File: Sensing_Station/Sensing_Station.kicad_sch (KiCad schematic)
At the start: 18 parts, among them J1 Conn_01x06_Pin, SW1 SW_Reed, U1 TMP35xS, U2 TLV172IDCK, U3 TLV172IDCK, U4 TLV172IDCK

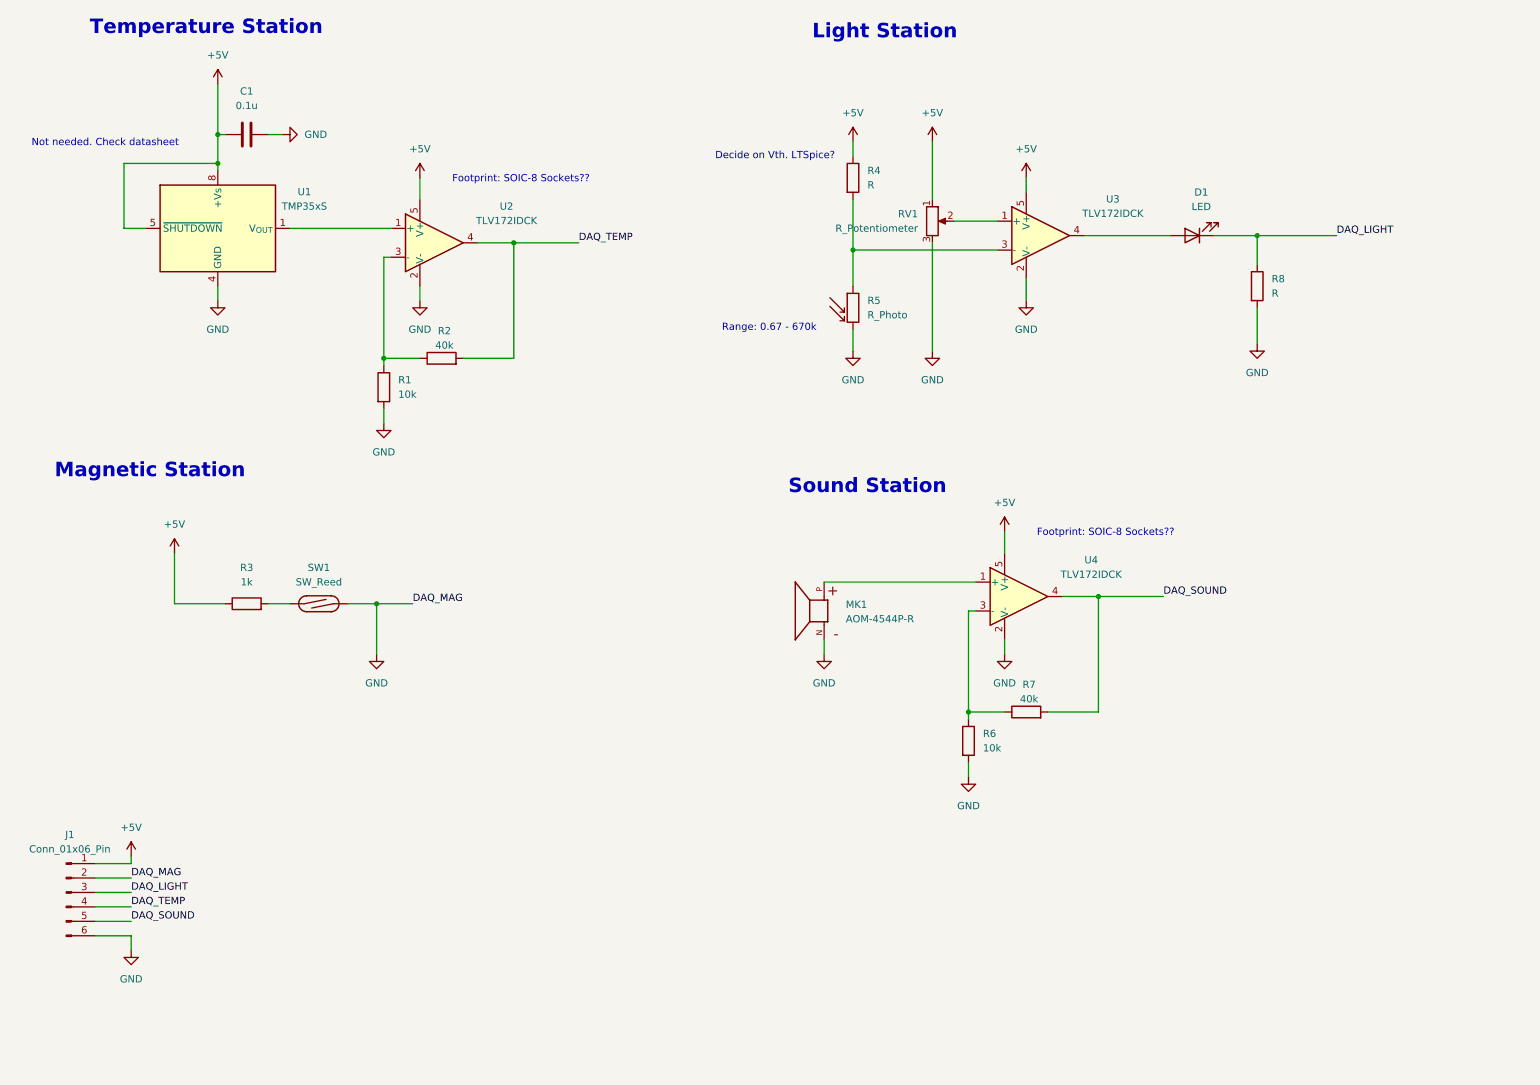
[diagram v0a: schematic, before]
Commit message: Añadido comparador doble y cambios. Falta BOM y listado final
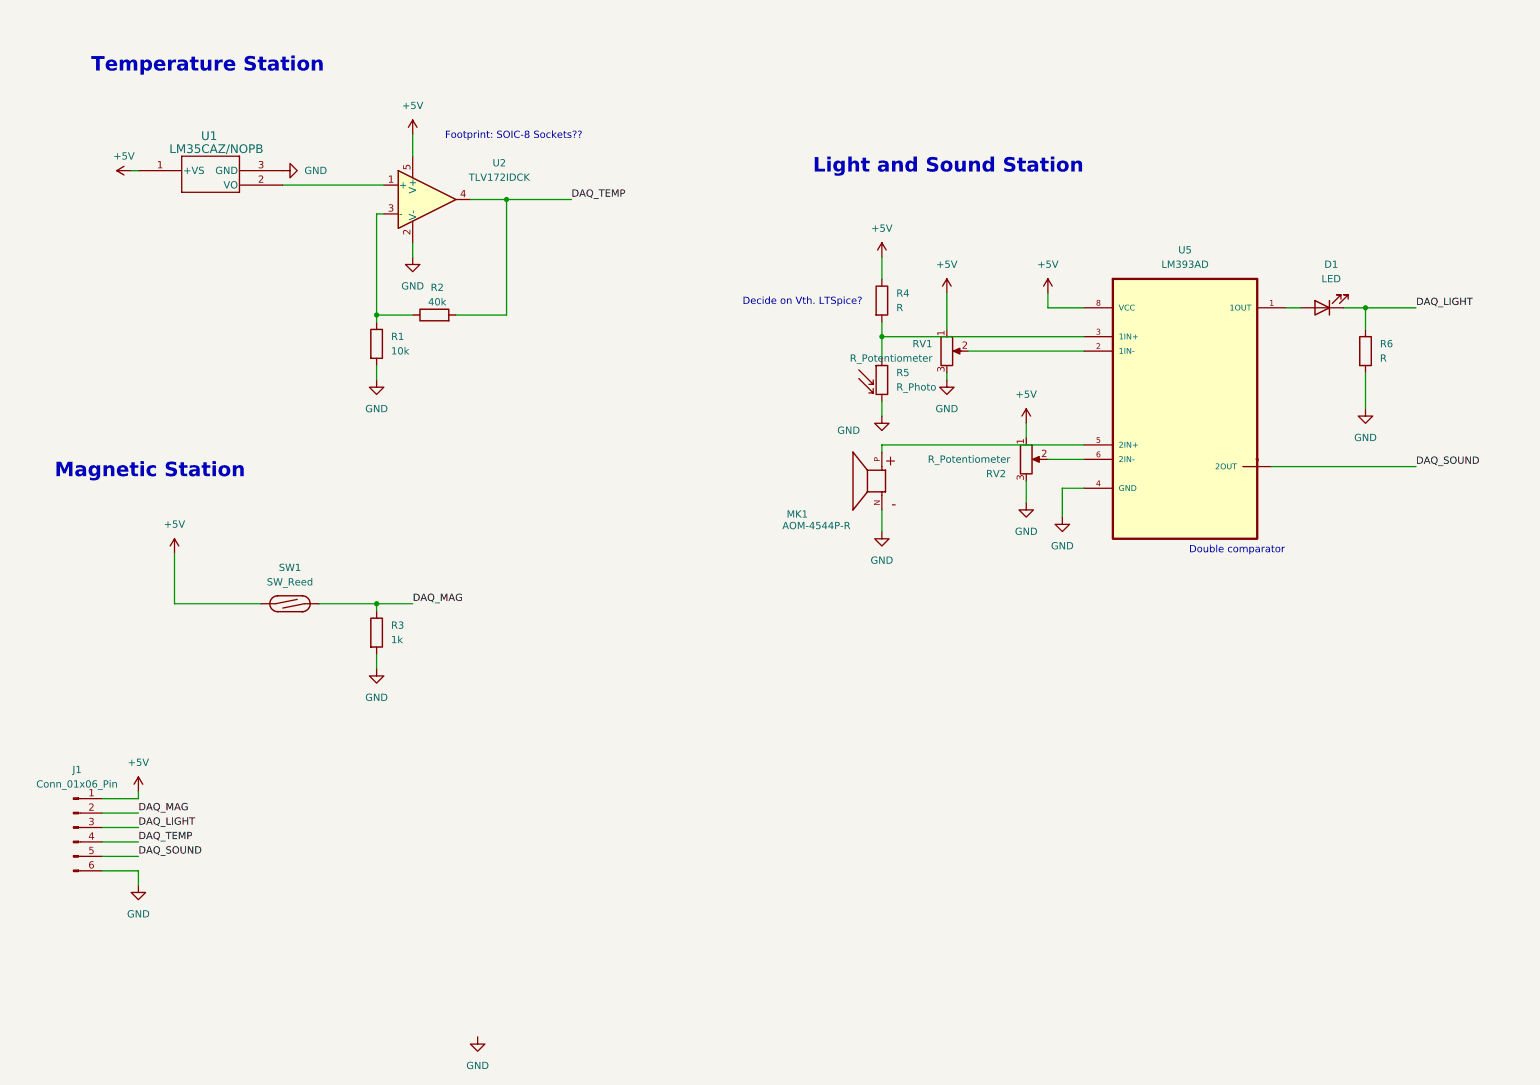
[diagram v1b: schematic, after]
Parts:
- removed C1: 0.1u, symbol Device:C
- removed R7: 40k, symbol Device:R
- removed R8: R, symbol Device:R
- removed U1: TMP35xS, Package_SO:SOIC-8_3.9x4.9mm_P1.27mm, symbol Sensor_Temperature:TMP36xS
- removed U3, U4: TLV172IDCK, Package_TO_SOT_SMD:SOT-353_SC-70-5, symbol Amplifier_Operational:TLV172IDCK
- added RV2: R_Potentiometer, symbol Device:R_Potentiometer
- added U1: LM35CAZ/NOPB, Z03A, symbol 2026-09-28_16-12-55:LM35CAZ_NOPB
- added U5: LM393AD, LM393AD:SOIC127P600X175-8N, symbol LM393AD:LM393AD
- R6: value 10k -> R
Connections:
- net +5V: now also SW1.1, RV2.1, U1.1 (+VS), U5.8 (VCC); no longer R3.1
- net DAQ_LIGHT: now also R6.1
- net DAQ_SOUND: now also U5.7 (2OUT)
- net GND: now also R3.2, RV2.3, U1.3 (GND), U5.4 (GND); no longer J1.2 (Pin_2), SW1.2
- net at RV1.2: now also U5.2 (1IN-)
- net at R4.2, R5.1: now also U5.3 (1IN+)
- net at D1.2 (A): now also U5.1 (1OUT)
- net at MK1.P: now also U5.5 (2IN+)
- net at U2.1 (+): now also U1.2 (VO)
- new net: RV2.2, U5.6 (2IN-)
- new net DAQ_MAG: J1.2 (Pin_2), R3.1, SW1.2
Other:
- note added: "Double comparator"
- note added: "Light and Sound Station"
- note removed: "Light Station"
- note removed: "Not needed. Check datasheet"
- note removed: "Range: 0.67 - 670k"
- note removed: "Sound Station"
- moved on the sheet: J1, R1, R2, SW1, U2

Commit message: Pull-ups a la salida del comparador doble
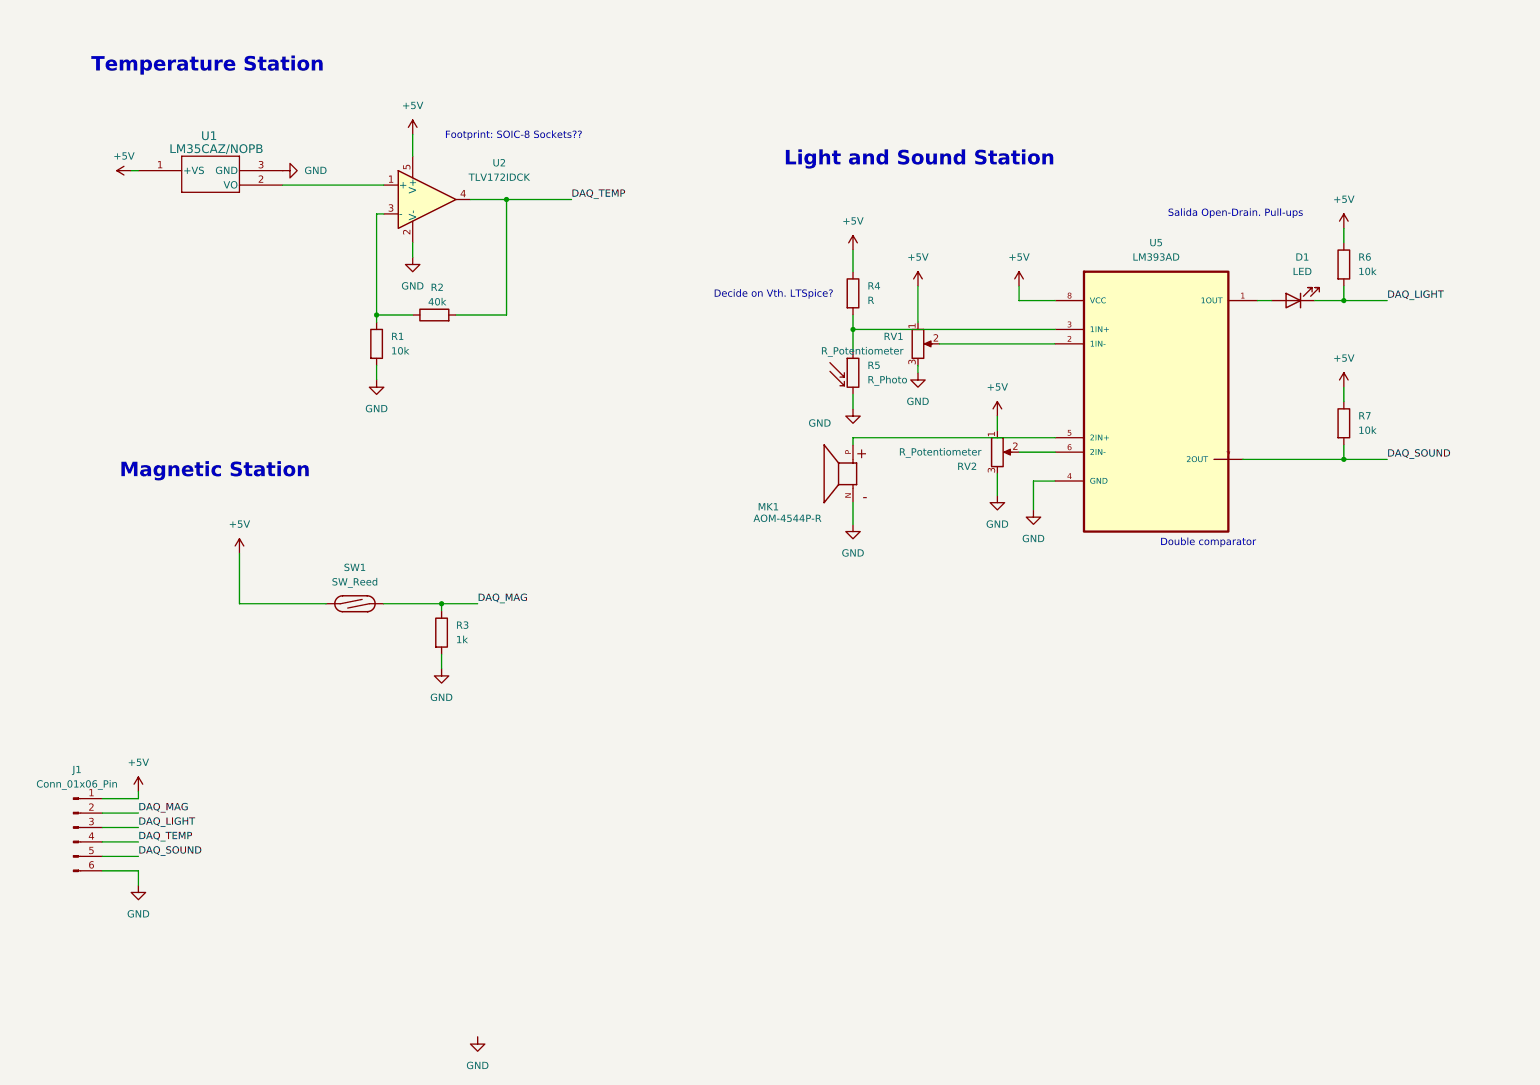
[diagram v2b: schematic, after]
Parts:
- added R7: 10k, symbol Device:R
- R6: value R -> 10k
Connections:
- net +5V: now also R6.1, R7.1
- net DAQ_LIGHT: now also R6.2; no longer R6.1
- net DAQ_SOUND: now also R7.2
- net GND: no longer R6.2
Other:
- note added: "Salida Open-Drain. Pull-ups"
- moved on the sheet: D1, MK1, R3, R4, R5, RV1, RV2, SW1, U5

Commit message: esquematico
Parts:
- removed MK1: AOM-4544P-R, AOM-4544P-R:MIC_AOM-4544P-R, symbol AOM-4544P-R:AOM-4544P-R
- removed R6, R7: 10k, symbol Device:R
- removed RV2: R_Potentiometer, symbol Device:R_Potentiometer
- removed U2: TLV172IDCK, Package_TO_SOT_SMD:SOT-353_SC-70-5, symbol Amplifier_Operational:TLV172IDCK
- removed U5: LM393AD, LM393AD:SOIC127P600X175-8N, symbol LM393AD:LM393AD
- added C1: 100nF, symbol Device:C
- added C2: 2.2uF, symbol Device:C
- added D3: LED, symbol Device:LED
- added D4: 1N4148W, Diode_SMD:D_SOD-123, symbol Diode:1N4148W
- added MK2: AOM-4544P-R, AOM-4544P-R:MIC_AOM-4544P-R, symbol AOM-4544P-R:AOM-4544P-R
- added Q1: NMOS, symbol Simulation_SPICE:NMOS
- added R10: 220, symbol Device:R
- added R11: R, symbol Device:R
- added R13: 30k, symbol Device:R
- added R8: 1k, symbol Device:R
- added R9: 2.2k, symbol Device:R
- added RV3: R_Potentiometer, symbol Device:R_Potentiometer
- added U3: LM358, symbol Amplifier_Operational:LM358
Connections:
- net +5V: now also R8.1, R9.1, U3.8 (V+)
- net DAQ_LIGHT: now also RV1.2, Q1.1 (D)
- net DAQ_SOUND: now also C2.1, D3.2 (A), D4.1 (K), R13.1
- net DAQ_TEMP: now also U3.7
- net GND: now also C2.2, MK2.N, Q1.3 (S), R10.2, R13.2, RV3.2, U3.4 (V-); no longer RV1.3
- net at R1.1, R2.1: now also U3.6 (-)
- net at R4.2, R5.1: now also Q1.2 (G)
- net at D1.2 (A): now also R8.2
- net at U1.2 (VO): now also U3.5 (+)
- new net: C1.1, MK2.P, R9.2
- new net: C1.2, U3.3 (+)
- new net: D4.2 (A), R11.2, U3.1
- new net: R11.1, RV3.1, U3.2 (-)
- new net: D3.1 (K), R10.1
- no-connect marks 0 -> 2
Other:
- note added: "LED ON-->DAQ=0V LED OFF-->DAQ=5V"
- note added: "Quizá haya que añadir otra resistendcia"
- note removed: "Double comparator"
- note removed: "Salida Open-Drain. Pull-ups"
